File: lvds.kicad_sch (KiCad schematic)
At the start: 96 parts, among them J15 Conn_FFC_Amphenol_62684-40210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

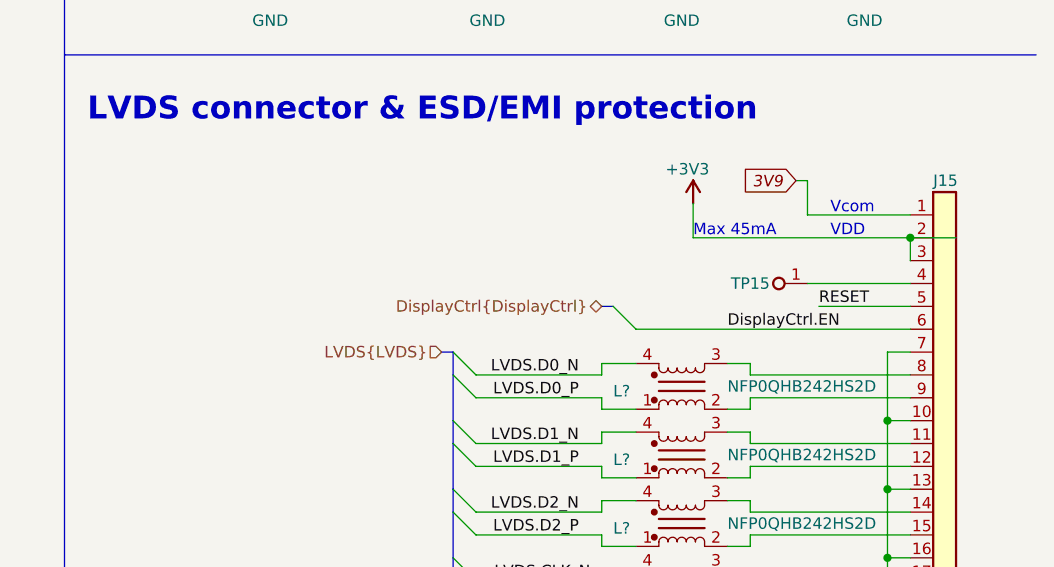
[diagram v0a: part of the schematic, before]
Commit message: [#54617] Add pull-up on DisplayCtrl.EN
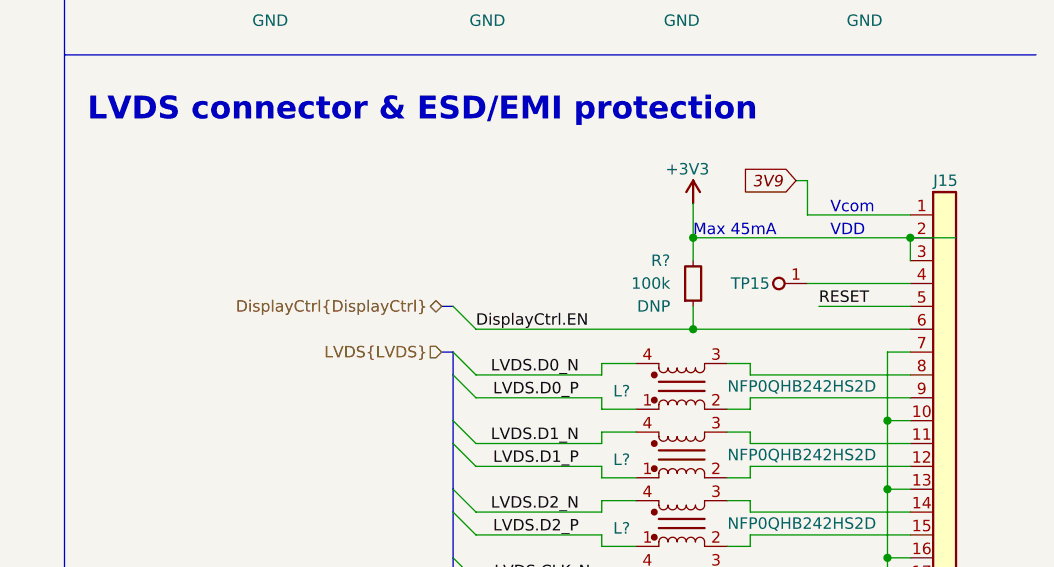
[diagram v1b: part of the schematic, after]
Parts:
- added R?: R_100k_0402, antmicro-footprints:R_0402_1005Metric, symbol antmicroResistors0402:R_100k_0402
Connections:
- net +3V3: now also R?.2
- net DisplayCtrl.EN: now also R?.1
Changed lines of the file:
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@@
   (junction (at 388.62 87.63) (diameter 0) (color 0 0 0 0)
   )
+  (junction (at 369.57 134.62) (diameter 0) (color 0 0 0 0)
+  )
+  (junction (at 369.57 124.46) (diameter 0) (color 0 0 0 0)
+  )
   (junction (at 391.16 175.26) (diameter 0) (color 0 0 0 0)
   )
@@
     (stroke (width 0) (type default) (color 0 0 0 0))
   )
-  (bus_entry (at 360.68 132.08) (size 2.54 2.54)
+  (bus_entry (at 342.9 132.08) (size 2.54 2.54)
     (stroke (width 0) (type default) (color 0 0 0 0))
   )
@@
     (stroke (width 0) (type default) (color 0 0 0 0))
   )
-  (wire (pts (xy 363.22 134.62) (xy 393.7 134.62))
+  (wire (pts (xy 345.44 134.62) (xy 369.57 134.62))
     (stroke (width 0) (type default) (color 0 0 0 0))
   )
@@
     (stroke (width 0) (type default) (color 0 0 0 0))
   )
-  (bus (pts (xy 359.41 132.08) (xy 360.68 132.08))
+  (bus (pts (xy 341.63 132.08) (xy 342.9 132.08))
     (stroke (width 0) (type default) (color 0 0 0 0))
   )
@@
     (stroke (width 0) (type default) (color 0 0 0 0))
   )
+  (wire (pts (xy 369.57 134.62) (xy 393.7 134.62))
+    (stroke (width 0) (type default) (color 0 0 0 0))
+  )
   (wire (pts (xy 317.5 45.72) (xy 317.5 44.45))
     (stroke (width 0) (type default) (color 0 0 0 0))
@@
     (stroke (width 0) (type default) (color 0 0 0 0))
   )
+  (wire (pts (xy 369.57 124.46) (xy 369.57 127))
+    (stroke (width 0) (type default) (color 0 0 0 0))
+  )
   (wire (pts (xy 346.71 87.63) (xy 346.71 88.9))
     (stroke (width 0) (type default) (color 0 0 0 0))
@@
     (stroke (width 0) (type default) (color 0 0 0 0))
   )
+  (wire (pts (xy 369.57 132.08) (xy 369.57 134.62))
+    (stroke (width 0) (type default) (color 0 0 0 0))
+  )
   (wire (pts (xy 208.28 224.79) (xy 205.74 224.79))
     (stroke (width 0) (type default) (color 0 0 0 0))
@@
     (effects (font (size 1.27 1.27)) (justify left bottom))
   )
-  (label "DisplayCtrl.EN" (at 373.38 134.62 0)
+  (label "DisplayCtrl.EN" (at 345.44 134.62 0)
     (effects (font (size 1.27 1.27)) (justify left bottom))
   )
@@
     (effects (font (size 1.27 1.27)) (justify right))
   )
-  (hierarchical_label "DisplayCtrl{DisplayCtrl}" (shape bidirectional) (at 359.41 132.08 180)
+  (hierarchical_label "DisplayCtrl{DisplayCtrl}" (shape bidirectional) (at 341.63 132.08 180)
     (effects (font (size 1.27 1.27)) (justify right))
   )
@@
     (pin "1")
   )
+  (symbol (lib_id "antmicroResistors0402:R_100k_0402") (at 369.57 132.08 90) (unit 1)
+    (in_bom yes) (on_board yes) (fields_autoplaced)
+    (property "Reference" "R?" (id 0) (at 367.03 126.9999 90)
+      (effects (font (size 1.27 1.27) (thickness 0.15)) (justify left))
+    )
+    (property "Value" "R_100k_0402" (id 1) (at 382.27 111.76 0)
+      (effects (font (size 1.27 1.27) (thickness 0.15)) (justify left bottom) hide)
+    )
+    (property "Footprint" "antmicro-footprints:R_0402_1005Metric" (id 2) (at 384.81 111.76 0)
+      (effects (font (size 1.27 1.27) (thickness 0.15)) (justify left bottom) hide)
+    )
+    (property "Datasheet" "https://www.bourns.com/docs/product-datasheets/cr.pdf" (id 3) (at 387.35 111.76 0)
+      (effects (font (size 1.27 1.27) (thickness 0.15)) (justify left bottom) hide)
+    )
+    (property "MPN" "CR0402-FX-1003GLF" (id 4) (at 389.89 111.76 0)
+      (effects (font (size 1.27 1.27) (thickness 0.15)) (justify left bottom) hide)
+    )
+    (property "Manufacturer" "Bourns" (id 5) (at 392.43 111.76 0)
+      (effects (font (size 1.27 1.27) (thickness 0.15)) (justify left bottom) hide)
+    )
+    (property "License" "Apache-2.0" (id 6) (at 394.97 111.76 0)
+      (effects (font (size 1.27 1.27) (thickness 0.15)) (justify left bottom) hide)
+    )
+    (property "Author" "Antmicro" (id 7) (at 397.51 111.76 0)
+      (effects (font (size 1.27 1.27) (thickness 0.15)) (justify left bottom) hide)
+    )
+    (property "Val" "100k" (id 8) (at 367.03 129.5399 90)
+      (effects (font (size 1.27 1.27) (thickness 0.15)) (justify left))
+    )
+    (property "Tolerance" "1%" (id 9) (at 379.73 111.76 0)
+      (effects (font (size 1.27 1.27)) (justify left bottom) hide)
+    )
+    (property "DNP" "DNP" (id 10) (at 367.03 132.0799 90)
+      (effects (font (size 1.27 1.27)) (justify left))
+    )
+    (pin "1")
+    (pin "2")
+  )
   (symbol (lib_id "antmicroCapacitors0402:C_100n_0402") (at 179.07 201.93 270) (mirror x) (unit 1)

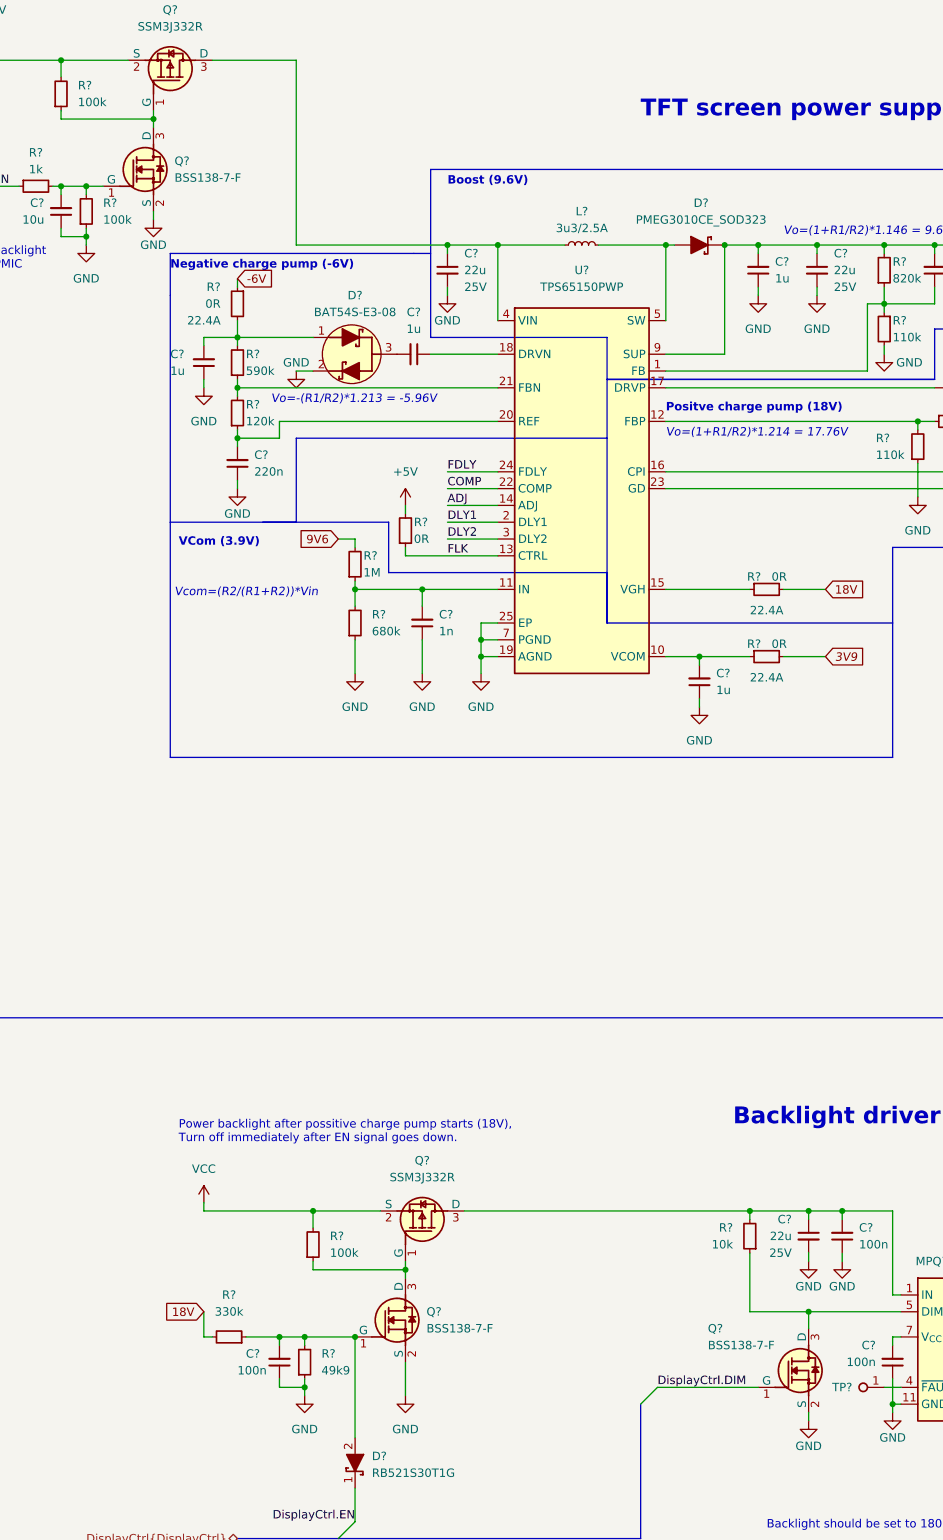
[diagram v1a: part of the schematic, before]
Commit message: [#54617] Change all NMOS to be single MPN
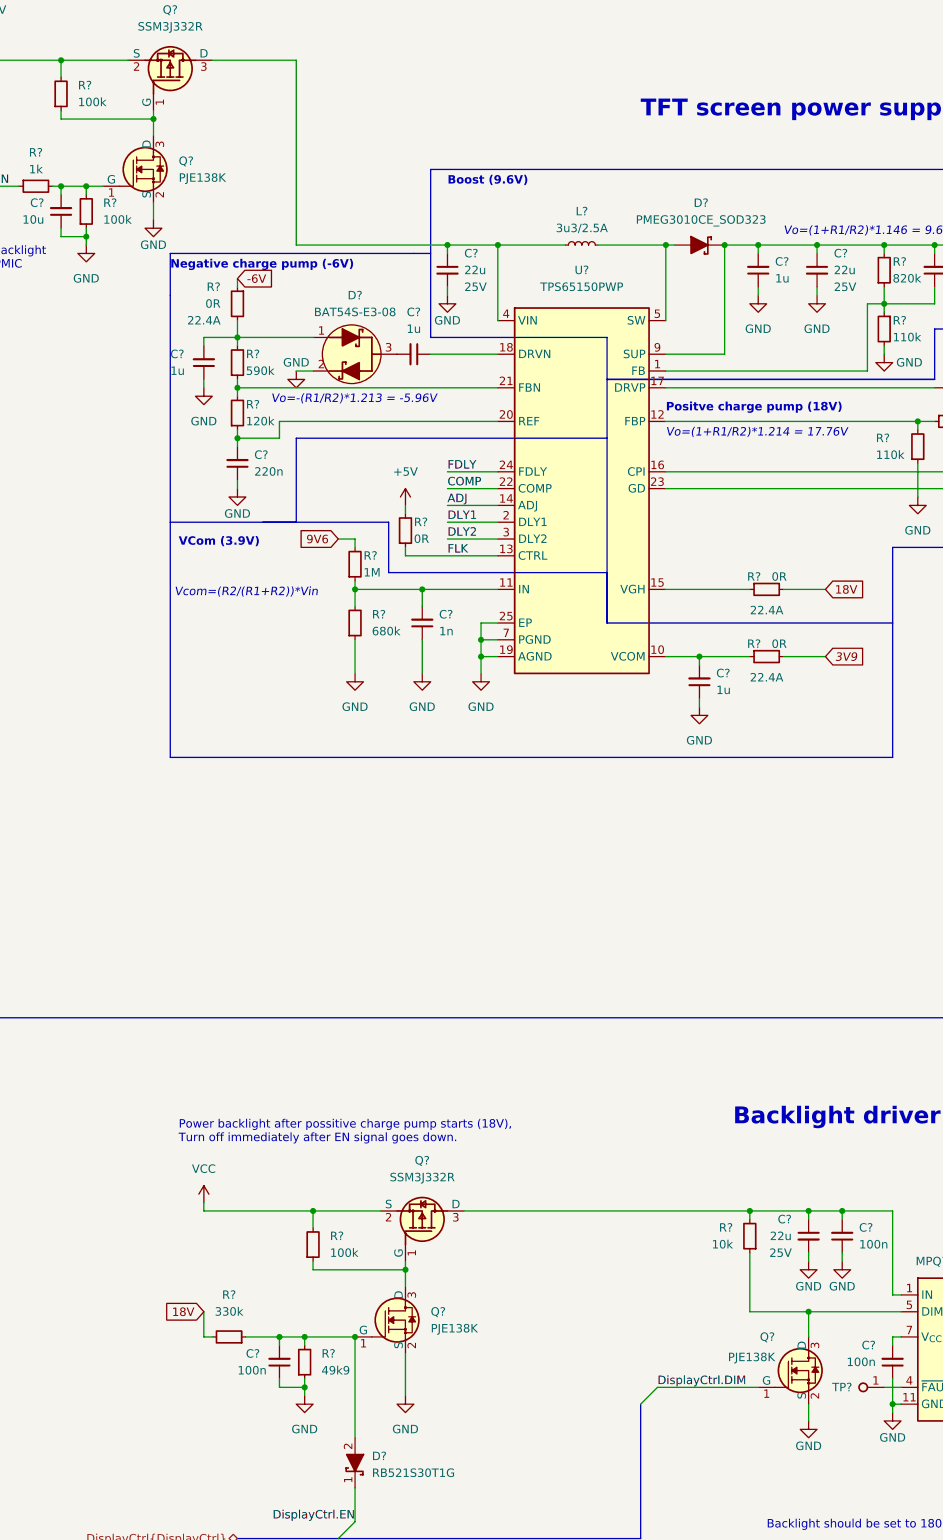
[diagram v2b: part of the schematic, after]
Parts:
- Q? (x3): value BSS138-7-F -> PJE138K; footprint antmicro-footprints:SOT-23-3 -> antmicro-footprints:SOT-523; symbol antmicroTransistorsFETsMOSFETsSingle:BSS138-7-F -> antmicroTransistorsFETsMOSFETsSingle:PJE138K; MPN BSS138-7-F -> PJE138K_R1_00001; Manufacturer Diodes Incorporated -> PANJIT
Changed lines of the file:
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@@
     (stroke (width 0) (type default) (color 0 0 0 0))
   )
-  (wire (pts (xy 113.03 218.44) (xy 113.03 223.52))
+  (wire (pts (xy 113.03 217.17) (xy 113.03 223.52))
     (stroke (width 0) (type default) (color 0 0 0 0))
   )
@@
     (stroke (width 0) (type default) (color 0 0 0 0))
   )
-  (wire (pts (xy 173.99 227.33) (xy 173.99 226.06))
-    (stroke (width 0) (type default) (color 0 0 0 0))
-  )
   (wire (pts (xy 346.71 85.09) (xy 346.71 87.63))
     (stroke (width 0) (type default) (color 0 0 0 0))
@@
     (stroke (width 0) (type default) (color 0 0 0 0))
   )
+  (wire (pts (xy 173.99 224.79) (xy 173.99 227.33))
+    (stroke (width 0) (type default) (color 0 0 0 0))
+  )
   (wire (pts (xy 119.38 91.44) (xy 127 91.44))
     (stroke (width 0) (type default) (color 0 0 0 0))
@@
     (stroke (width 0) (type default) (color 0 0 0 0))
   )
-  (wire (pts (xy 74.93 44.45) (xy 74.93 45.72))
+  (wire (pts (xy 74.93 43.18) (xy 74.93 45.72))
     (stroke (width 0) (type default) (color 0 0 0 0))
   )
@@
     (stroke (width 0) (type default) (color 0 0 0 0))
   )
-  (wire (pts (xy 173.99 210.82) (xy 173.99 213.36))
+  (wire (pts (xy 173.99 210.82) (xy 173.99 214.63))
     (stroke (width 0) (type default) (color 0 0 0 0))
   )
@@
     (stroke (width 0) (type default) (color 0 0 0 0))
   )
-  (wire (pts (xy 113.03 204.47) (xy 113.03 205.74))
+  (wire (pts (xy 113.03 204.47) (xy 113.03 207.01))
     (stroke (width 0) (type default) (color 0 0 0 0))
   )
@@
     (stroke (width 0) (type default) (color 0 0 0 0))
   )
-  (wire (pts (xy 74.93 30.48) (xy 74.93 31.75))
+  (wire (pts (xy 74.93 30.48) (xy 74.93 33.02))
     (stroke (width 0) (type default) (color 0 0 0 0))
   )
@@
     (pin "2")
   )
-  (symbol (lib_id "antmicroTransistorsFETsMOSFETsSingle:BSS138-7-F") (at 166.37 222.25 0) (unit 1)
+  (symbol (lib_id "antmicroTransistorsFETsMOSFETsSingle:PJE138K") (at 166.37 222.25 0) (unit 1)
     (in_bom yes) (on_board yes)
-    (property "Reference" "Q?" (id 0) (at 158.75 213.36 0)
-      (effects (font (size 1.27 1.27) (thickness 0.15)) (justify left))
+    (property "Reference" "Q?" (id 0) (at 168.91 214.63 0)
+      (effects (font (size 1.27 1.27) (thickness 0.15)) (justify right))
     )
-    (property "Value" "BSS138-7-F" (id 1) (at 158.75 215.9 0)
-      (effects (font (size 1.27 1.27) (thickness 0.15)) (justify left))
+    (property "Value" "PJE138K" (id 1) (at 168.91 218.44 0)
+      (effects (font (size 1.27 1.27) (thickness 0.15)) (justify right bottom))
     )
-    (property "Footprint" "antmicro-footprints:SOT-23-3" (id 2) (at 189.23 229.87 0)
+    (property "Footprint" "antmicro-footprints:SOT-523" (id 2) (at 189.23 233.68 0)
       (effects (font (size 1.27 1.27) (thickness 0.15)) (justify left bottom) hide)
     )
-    (property "Datasheet" "https://www.diodes.com/assets/Datasheets/ds30144.pdf" (id 3) (at 189.23 232.41 0)
+    (property "Datasheet" "https://www.mouser.com/datasheet/2/1057/PJE138K-1876698.pdf" (id 3) (at 189.23 236.22 0)
       (effects (font (size 1.27 1.27) (thickness 0.15)) (justify left bottom) hide)
     )
-    (property "MPN" "BSS138-7-F" (id 4) (at 189.23 234.95 0)
+    (property "MPN" "PJE138K_R1_00001" (id 4) (at 189.23 238.76 0)
       (effects (font (size 1.27 1.27) (thickness 0.15)) (justify left bottom) hide)
     )
-    (property "Manufacturer" "Diodes Incorporated" (id 5) (at 189.23 237.49 0)
+    (property "Manufacturer" "PANJIT" (id 5) (at 189.23 241.3 0)
       (effects (font (size 1.27 1.27) (thickness 0.15)) (justify left bottom) hide)
     )
-    (property "Author" "Antmicro" (id 6) (at 189.23 240.03 0)
+    (property "Author" "Antmicro" (id 6) (at 189.23 243.84 0)
       (effects (font (size 1.27 1.27) (thickness 0.15)) (justify left bottom) hide)
     )
-    (property "License" "Apache-2.0" (id 7) (at 189.23 242.57 0)
+    (property "License" "Apache-2.0" (id 7) (at 189.23 246.38 0)
       (effects (font (size 1.27 1.27) (thickness 0.15)) (justify left bottom) hide)
     )
@@
     (pin "1")
   )
-  (symbol (lib_id "antmicroTransistorsFETsMOSFETsSingle:BSS138-7-F") (at 105.41 214.63 0) (unit 1)
+  (symbol (lib_id "antmicroTransistorsFETsMOSFETsSingle:PJE138K") (at 105.41 214.63 0) (unit 1)
     (in_bom yes) (on_board yes) (fields_autoplaced)
-    (property "Reference" "Q?" (id 0) (at 116.205 210.8199 0)
+    (property "Reference" "Q?" (id 0) (at 116.84 210.8199 0)
       (effects (font (size 1.27 1.27) (thickness 0.15)) (justify left))
     )
-    (property "Value" "BSS138-7-F" (id 1) (at 116.205 213.3599 0)
+    (property "Value" "PJE138K" (id 1) (at 116.84 213.3599 0)
       (effects (font (size 1.27 1.27) (thickness 0.15)) (justify left))
     )
-    (property "Footprint" "antmicro-footprints:SOT-23-3" (id 2) (at 128.27 222.25 0)
+    (property "Footprint" "antmicro-footprints:SOT-523" (id 2) (at 128.27 226.06 0)
       (effects (font (size 1.27 1.27) (thickness 0.15)) (justify left bottom) hide)
     )
-    (property "Datasheet" "https://www.diodes.com/assets/Datasheets/ds30144.pdf" (id 3) (at 128.27 224.79 0)
+    (property "Datasheet" "https://www.mouser.com/datasheet/2/1057/PJE138K-1876698.pdf" (id 3) (at 128.27 228.6 0)
       (effects (font (size 1.27 1.27) (thickness 0.15)) (justify left bottom) hide)
     )
-    (property "MPN" "BSS138-7-F" (id 4) (at 128.27 227.33 0)
+    (property "MPN" "PJE138K_R1_00001" (id 4) (at 128.27 231.14 0)
       (effects (font (size 1.27 1.27) (thickness 0.15)) (justify left bottom) hide)
     )
-    (property "Manufacturer" "Diodes Incorporated" (id 5) (at 128.27 229.87 0)
+    (property "Manufacturer" "PANJIT" (id 5) (at 128.27 233.68 0)
       (effects (font (size 1.27 1.27) (thickness 0.15)) (justify left bottom) hide)
     )
-    (property "Author" "Antmicro" (id 6) (at 128.27 232.41 0)
+    (property "Author" "Antmicro" (id 6) (at 128.27 236.22 0)
       (effects (font (size 1.27 1.27) (thickness 0.15)) (justify left bottom) hide)
     )
-    (property "License" "Apache-2.0" (id 7) (at 128.27 234.95 0)
+    (property "License" "Apache-2.0" (id 7) (at 128.27 238.76 0)
       (effects (font (size 1.27 1.27) (thickness 0.15)) (justify left bottom) hide)
     )
@@
     (pin "2")
   )
-  (symbol (lib_id "antmicroTransistorsFETsMOSFETsSingle:BSS138-7-F") (at 67.31 40.64 0) (unit 1)
+  (symbol (lib_id "antmicroTransistorsFETsMOSFETsSingle:PJE138K") (at 67.31 40.64 0) (unit 1)
     (in_bom yes) (on_board yes) (fields_autoplaced)
-    (property "Reference" "Q?" (id 0) (at 78.105 36.8299 0)
+    (property "Reference" "Q?" (id 0) (at 78.74 36.8299 0)
       (effects (font (size 1.27 1.27) (thickness 0.15)) (justify left))
     )
-    (property "Value" "BSS138-7-F" (id 1) (at 78.105 39.3699 0)
+    (property "Value" "PJE138K" (id 1) (at 78.74 39.3699 0)
       (effects (font (size 1.27 1.27) (thickness 0.15)) (justify left))
     )
-    (property "Footprint" "antmicro-footprints:SOT-23-3" (id 2) (at 90.17 48.26 0)
+    (property "Footprint" "antmicro-footprints:SOT-523" (id 2) (at 90.17 52.07 0)
       (effects (font (size 1.27 1.27) (thickness 0.15)) (justify left bottom) hide)
     )
-    (property "Datasheet" "https://www.diodes.com/assets/Datasheets/ds30144.pdf" (id 3) (at 90.17 50.8 0)
+    (property "Datasheet" "https://www.mouser.com/datasheet/2/1057/PJE138K-1876698.pdf" (id 3) (at 90.17 54.61 0)
       (effects (font (size 1.27 1.27) (thickness 0.15)) (justify left bottom) hide)
     )
-    (property "MPN" "BSS138-7-F" (id 4) (at 90.17 53.34 0)
+    (property "MPN" "PJE138K_R1_00001" (id 4) (at 90.17 57.15 0)
       (effects (font (size 1.27 1.27) (thickness 0.15)) (justify left bottom) hide)
     )
-    (property "Manufacturer" "Diodes Incorporated" (id 5) (at 90.17 55.88 0)
+    (property "Manufacturer" "PANJIT" (id 5) (at 90.17 59.69 0)
       (effects (font (size 1.27 1.27) (thickness 0.15)) (justify left bottom) hide)
     )
-    (property "Author" "Antmicro" (id 6) (at 90.17 58.42 0)
+    (property "Author" "Antmicro" (id 6) (at 90.17 62.23 0)
       (effects (font (size 1.27 1.27) (thickness 0.15)) (justify left bottom) hide)
     )
-    (property "License" "Apache-2.0" (id 7) (at 90.17 60.96 0)
+    (property "License" "Apache-2.0" (id 7) (at 90.17 64.77 0)
       (effects (font (size 1.27 1.27) (thickness 0.15)) (justify left bottom) hide)
     )
